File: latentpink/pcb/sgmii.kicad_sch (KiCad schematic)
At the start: 90 parts, among them J22 BEL_FUSE_0845-2R1T-E4, U2 XC7K160T-2FBG484C, U5 DP83867, U6 DP83867, U7 ECS-1612MV-250-CN-TR, U8 ECS-1612MV-250-CN-TR

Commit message: Finished initial schematic, ready for design review
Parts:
- added C477, C478, C479, C480: 22 uF, azonenberg_pcb:EIA_1206_CAP_NOSILK, symbol device:C
- added FB10, FB11: CIS21J121NE, azonenberg_pcb:EIA_0805_INDUCTOR_NOSILK, symbol passive-azonenberg:INDUCTOR_PWROUT
- added TP26, TP27: U.FL, azonenberg_pcb:CONN_U.FL_TE_1909763-1, symbol conn:CONN_COAXIAL
- R112, R113, R114, R119, R120, R121: footprint (none) -> azonenberg_pcb:EIA_0402_RES_NOSILK
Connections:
- net 1V8: now also C478.1, FB11.2
- net 2V5: now also C477.1, FB10.2
- net DP_A1V8: now also C480.1, FB11.1, TP27.1 (In)
- net DP_A2V5: now also C479.1, FB10.1, TP26.1 (In)
- net ETH12_A_N: no longer J22.15 (BI_DA_P)
- net ETH12_A_P: now also J22.15 (BI_DA_P)
- net GND: now also C477.2, C478.2, C479.2, C480.2, TP26.2 (Ext), TP27.2 (Ext)
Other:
- note added: "Filtering for analog rails"
- note removed: "TODO: power filtering"

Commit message: Rearranged all unplaced components and grouped by functional subsystem
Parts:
- removed R112: 1.5K, azonenberg_pcb:EIA_0402_RES_NOSILK, symbol device:R
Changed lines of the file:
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@@
-    (stroke (width 0) (type default) (color 0 0 0 0))
-  )
-  (wire (pts (xy 143.51 102.87) (xy 158.75 102.87))
     (stroke (width 0) (type default) (color 0 0 0 0))
   )
@@
   )
   (wire (pts (xy 341.63 200.66) (xy 341.63 203.2))
-    (stroke (width 0) (type default) (color 0 0 0 0))
-  )
-  (wire (pts (xy 135.89 102.87) (xy 135.89 107.95))
     (stroke (width 0) (type default) (color 0 0 0 0))
   )
@@
       (effects (font (size 1.27 1.27)) hide)
     )
-    (pin "1")
-    (pin "2")
-  )
-  (symbol (lib_id "device:R") (at 139.7 102.87 90) (unit 1)
-    (in_bom yes) (on_board yes) (fields_autoplaced)
-    (property "Reference" "R112" (id 0) (at 139.7 98.1542 90))
-    (property "Value" "1.5K" (id 1) (at 139.7 100.6911 90))
-    (property "Footprint" "azonenberg_pcb:EIA_0402_RES_NOSILK" (id 2) (at 139.7 104.648 90)
-      (effects (font (size 1.27 1.27)) hide)
-    )
-    (property "Datasheet" "" (id 3) (at 139.7 102.87 0)
-      (effects (font (size 1.27 1.27)) hide)
-    )

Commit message: Routed upper SGMII PHY except for bus to FPGA
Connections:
- net ETH12_LED_0_1V8 is gone; now on net ETH12_LED0_1V8: R139.1, R140.1
- net ETH13_LED_0_1V8 is gone; now on net ETH13_LED0_1V8: R143.1, R144.1
- net 1V8: no longer R113.1, R119.1, R120.1, R137.2, R139.2, R141.2, R143.2, R145.2, R147.2
- net 1V8_IO: now also R113.1, R119.1, R120.1, R137.2, R139.2, R141.2, R143.2, R145.2, R147.2
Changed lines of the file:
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@@
   (paper "A3")
   (title_block
-    (date "2023-05-27")
+    (date "2023-05-28")
     (rev "0.1")
     (company "Antikernel Labs")
@@
     (effects (font (size 1.27 1.27)) (justify right bottom))
   )
-  (label "1V8" (at 236.22 86.36 0)
+  (label "1V8_IO" (at 236.22 86.36 0)
     (effects (font (size 1.27 1.27)) (justify left bottom))
   )
@@
     (effects (font (size 1.27 1.27)) (justify right bottom))
   )
-  (label "1V8" (at 236.22 236.22 0)
+  (label "1V8_IO" (at 236.22 236.22 0)
     (effects (font (size 1.27 1.27)) (justify left bottom))
   )
@@
     (effects (font (size 1.27 1.27)) (justify right bottom))
   )
-  (label "1V8" (at 236.22 210.82 0)
+  (label "1V8_IO" (at 236.22 210.82 0)
     (effects (font (size 1.27 1.27)) (justify left bottom))
   )
@@
     (effects (font (size 1.27 1.27)) (justify left bottom))
   )
-  (label "ETH13_LED_0_1V8" (at 228.6 210.82 180)
+  (label "ETH13_LED0_1V8" (at 228.6 210.82 180)
     (effects (font (size 1.27 1.27)) (justify right bottom))
   )
@@
     (effects (font (size 1.27 1.27)) (justify right bottom))
   )
-  (label "1V8" (at 236.22 223.52 0)
+  (label "1V8_IO" (at 236.22 223.52 0)
     (effects (font (size 1.27 1.27)) (justify left bottom))
   )
@@
     (effects (font (size 1.27 1.27)) (justify left bottom))
   )
-  (label "1V8" (at 135.89 107.95 180)
+  (label "1V8_IO" (at 135.89 107.95 180)
     (effects (font (size 1.27 1.27)) (justify right bottom))
   )
@@
     (effects (font (size 1.27 1.27)) (justify right bottom))
   )
-  (label "ETH12_LED_0_1V8" (at 228.6 99.06 180)
+  (label "ETH12_LED0_1V8" (at 228.6 99.06 180)
     (effects (font (size 1.27 1.27)) (justify right bottom))
   )
@@
     (effects (font (size 1.27 1.27)) (justify right bottom))
   )
-  (label "1V8" (at 236.22 198.12 0)
+  (label "1V8_IO" (at 236.22 198.12 0)
     (effects (font (size 1.27 1.27)) (justify left bottom))
   )
@@
     (effects (font (size 1.27 1.27)) (justify right bottom))
   )
-  (label "1V8" (at 236.22 99.06 0)
+  (label "1V8_IO" (at 236.22 99.06 0)
     (effects (font (size 1.27 1.27)) (justify left bottom))
   )
@@
     (effects (font (size 1.27 1.27)) (justify left bottom))
   )
-  (label "1V8" (at 135.89 222.25 180)
-    (effects (font (size 1.27 1.27)) (justify right bottom))
-  )
+  (label "1V8_IO" (at 135.89 222.25 180)
+    (effects (font (size 1.27 1.27)) (justify right bottom))
+  )

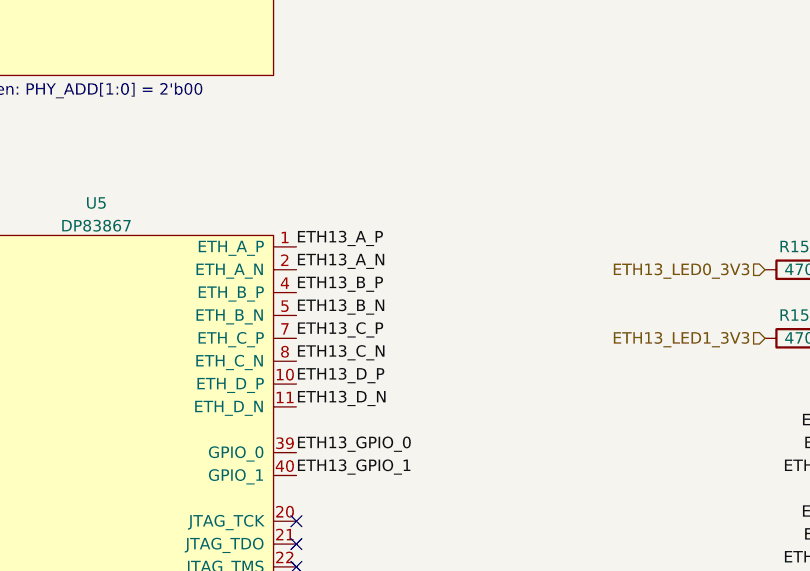
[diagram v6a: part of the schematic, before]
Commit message: Hooked up some more PHY stuff plus management UART transceiver
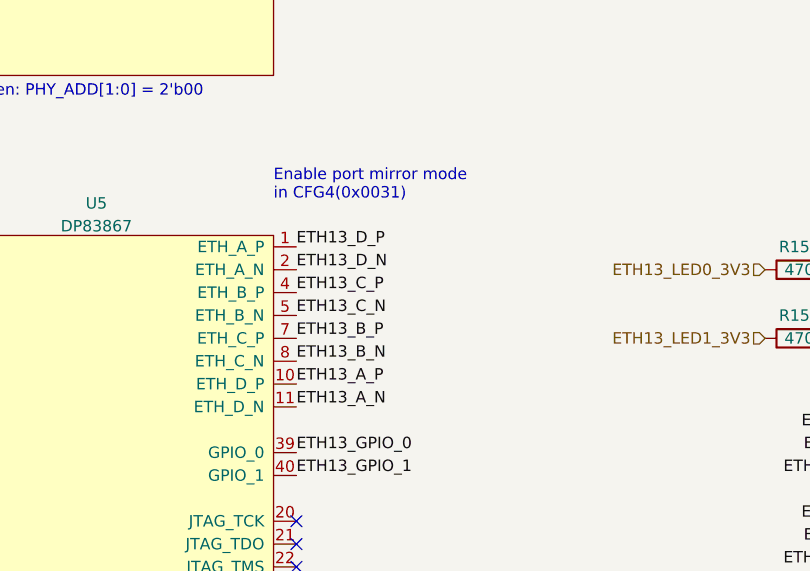
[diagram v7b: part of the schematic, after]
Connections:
- net ETH13_A_N: now also U5.11 (ETH_D_N); no longer U5.2 (ETH_A_N)
- net ETH13_A_P: now also U5.10 (ETH_D_P); no longer U5.1 (ETH_A_P)
- net ETH13_B_N: now also U5.8 (ETH_C_N); no longer U5.5 (ETH_B_N)
- net ETH13_B_P: now also U5.7 (ETH_C_P); no longer U5.4 (ETH_B_P)
- net ETH13_C_N: now also U5.5 (ETH_B_N); no longer U5.8 (ETH_C_N)
- net ETH13_C_P: now also U5.4 (ETH_B_P); no longer U5.7 (ETH_C_P)
- net ETH13_D_N: now also U5.2 (ETH_A_N); no longer U5.11 (ETH_D_N)
- net ETH13_D_P: now also U5.1 (ETH_A_P); no longer U5.10 (ETH_D_P)
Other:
- note added: "Enable port mirror mode in CFG4(0x0031)"
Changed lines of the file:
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@@
+    (effects (font (size 1.27 1.27)) (justify left bottom))
+  )
+  (text "Enable port mirror mode\nin CFG4(0x0031)" (at 200.66 135.89 0)
     (effects (font (size 1.27 1.27)) (justify left bottom))
   )
@@
     (effects (font (size 1.27 1.27)) (justify right bottom))
   )
-  (label "ETH13_A_N" (at 203.2 143.51 0)
+  (label "ETH13_A_N" (at 203.2 158.75 0)
     (effects (font (size 1.27 1.27)) (justify left bottom))
   )
@@
     (effects (font (size 1.27 1.27)) (justify right bottom))
   )
-  (label "ETH13_D_N" (at 203.2 158.75 0)
+  (label "ETH13_D_N" (at 203.2 143.51 0)
     (effects (font (size 1.27 1.27)) (justify left bottom))
   )
@@
     (effects (font (size 1.27 1.27)) (justify left bottom))
   )
-  (label "ETH13_C_P" (at 203.2 151.13 0)
+  (label "ETH13_C_P" (at 203.2 146.05 0)
     (effects (font (size 1.27 1.27)) (justify left bottom))
   )
@@
     (effects (font (size 1.27 1.27)) (justify right bottom))
   )
-  (label "ETH13_A_P" (at 203.2 140.97 0)
+  (label "ETH13_A_P" (at 203.2 156.21 0)
     (effects (font (size 1.27 1.27)) (justify left bottom))
   )
@@
     (effects (font (size 1.27 1.27)) (justify left bottom))
   )
-  (label "ETH13_C_N" (at 203.2 153.67 0)
+  (label "ETH13_C_N" (at 203.2 148.59 0)
     (effects (font (size 1.27 1.27)) (justify left bottom))
   )
@@
     (effects (font (size 1.27 1.27)) (justify left bottom))
   )
-  (label "ETH13_B_P" (at 203.2 146.05 0)
+  (label "ETH13_B_P" (at 203.2 151.13 0)
     (effects (font (size 1.27 1.27)) (justify left bottom))
   )
@@
     (effects (font (size 1.27 1.27)) (justify right bottom))
   )
-  (label "ETH13_D_P" (at 203.2 156.21 0)
+  (label "ETH13_D_P" (at 203.2 140.97 0)
     (effects (font (size 1.27 1.27)) (justify left bottom))
   )
@@
     (effects (font (size 1.27 1.27)) (justify right bottom))
   )
-  (label "ETH13_B_N" (at 203.2 148.59 0)
+  (label "ETH13_B_N" (at 203.2 153.67 0)
     (effects (font (size 1.27 1.27)) (justify left bottom))
   )
@@
   )
   (symbol (lib_id "device:C") (at 340.36 180.34 0) (unit 1)
-    (in_bom yes) (on_board yes) (fields_autoplaced)
+    (in_bom yes) (on_board yes)
     (property "Reference" "C372" (id 0) (at 343.281 179.4315 0)
       (effects (font (size 1.27 1.27)) (justify left))
